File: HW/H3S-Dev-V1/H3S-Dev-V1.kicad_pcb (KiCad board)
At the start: 2 copper layers, 85 x 56 mm, 33 parts, among them J1 USB_C_Receptacle_USB2.0_16P, J2 Conn_01x02_Socket, J3 Conn_Coaxial, Q1 DMP3099L, U1 Ai-Thinker-Ra-01, U2 LTC4054ES5-4.2, U3 USBLC6-2SC6, U4 ESP32-S3-WROOM-1, U5 SY8089AAAC

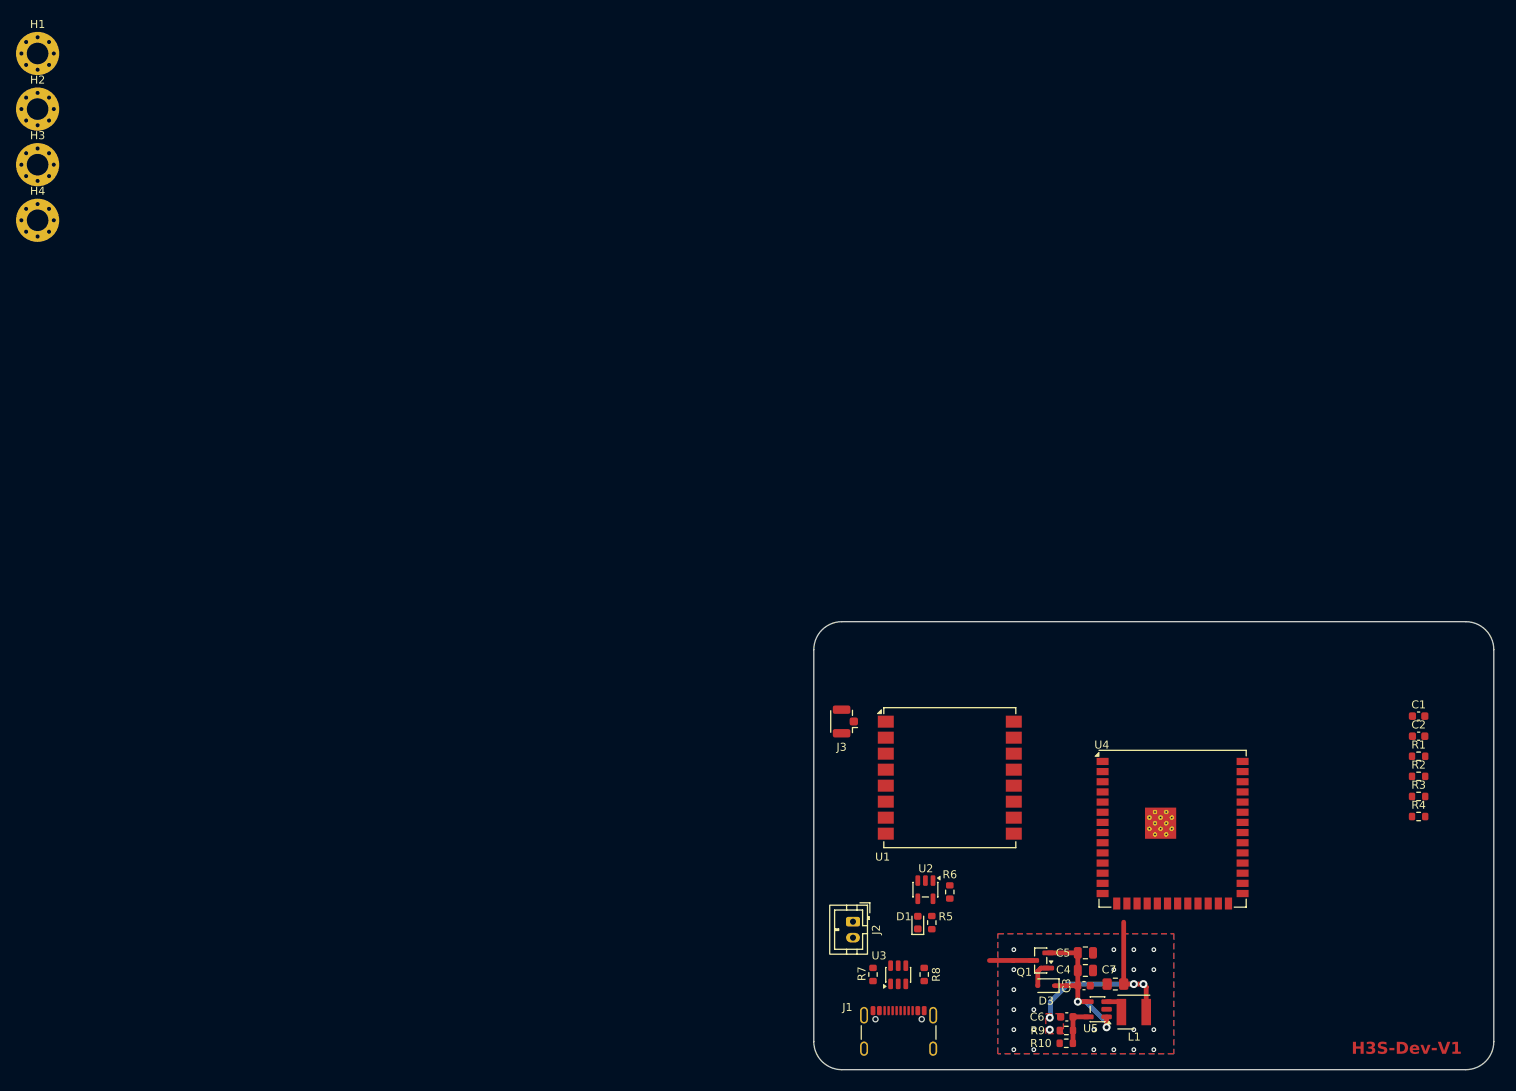
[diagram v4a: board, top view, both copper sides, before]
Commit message: LoRa, Reset and some more routing
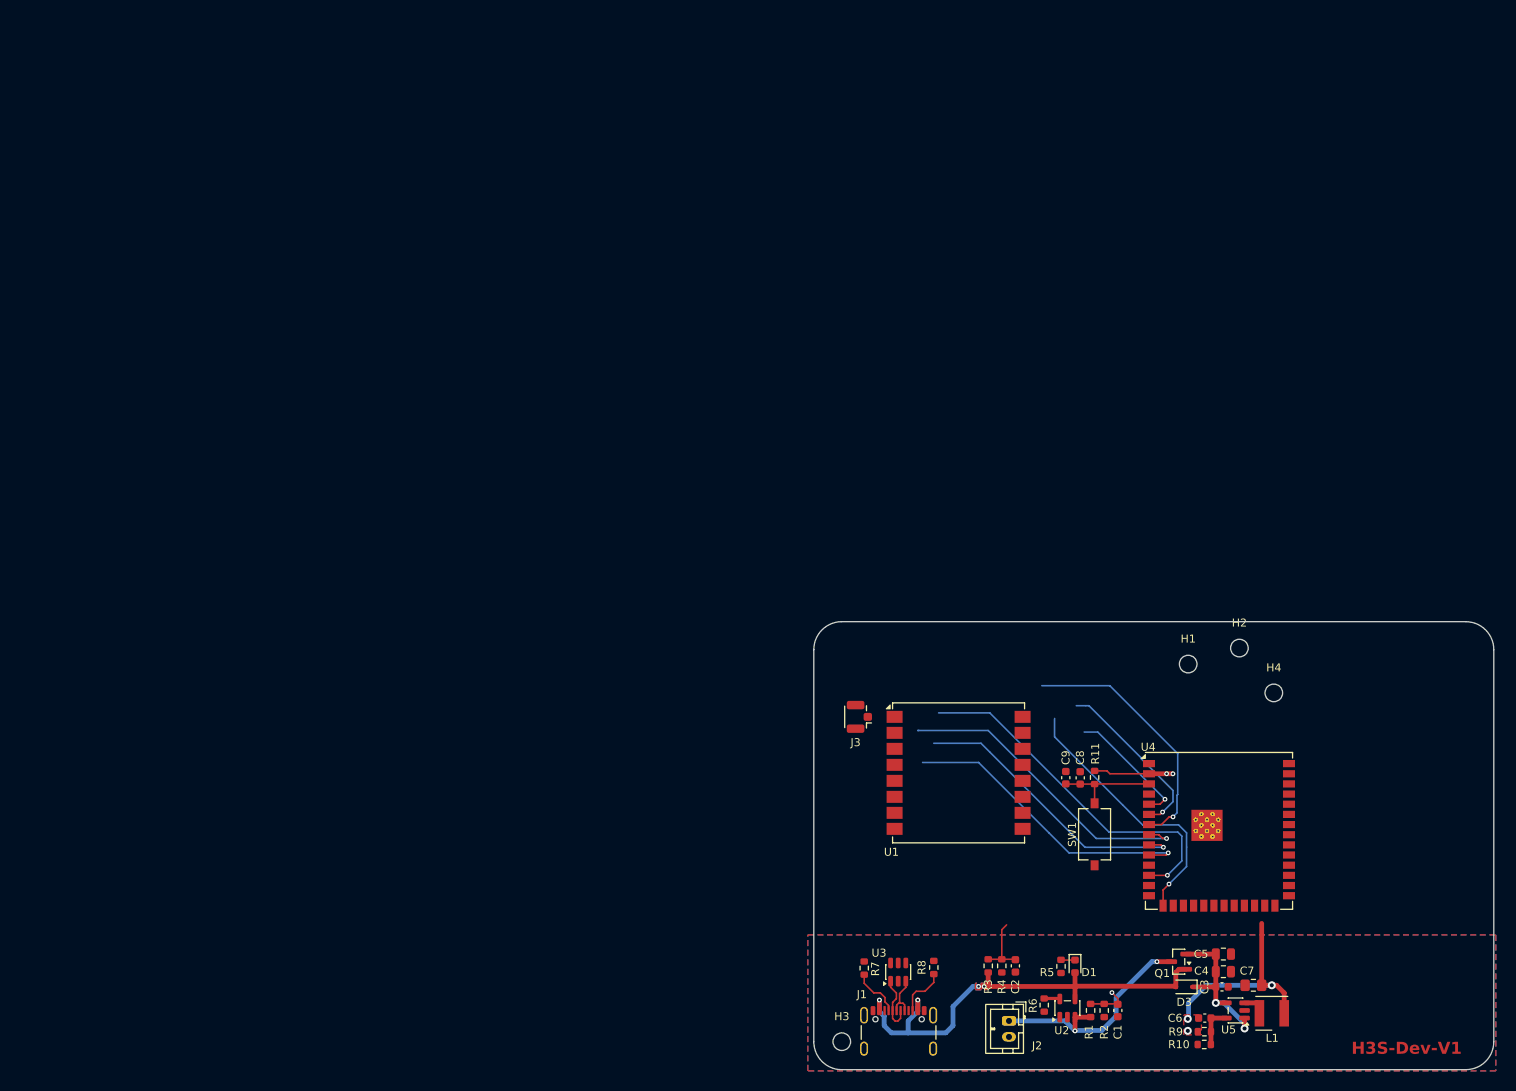
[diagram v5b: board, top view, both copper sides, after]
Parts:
- added C8: 1u, Capacitor_SMD:C_0603_1608Metric, F.Cu at (133.3, 93.5)
- added C9: 100n, Capacitor_SMD:C_0603_1608Metric, F.Cu at (131.5, 93.5)
- added R11: 10k, Resistor_SMD:R_0603_1608Metric, F.Cu at (135.1, 93.5)
- added SW1: SW_Push, Button_Switch_SMD:SW_Tactile_SPST_NO_Straight_CK_PTS636Sx25SMTRLFS, F.Cu at (135.1, 100.6)
- H1, H2, H3, H4: value MountingHole_Pad_MP -> MountingHole; footprint MountingHole:MountingHole_2.7mm_M2.5_Pad_Via -> MountingHole:MountingHole_2.2mm_M2
- moved H4 165.4 mm to (157.5, 82.9)
- moved H2 164.6 mm to (153.2, 77.3)
- moved H1 162.8 mm to (146.8, 79.3)
- moved H3 148.7 mm to (103.5, 126.5)
- moved C2 58.0 mm to (125.2, 117.0), turned to -90 degrees
- moved R3 57.8 mm to (121.8, 117.0), turned to 90 degrees
- moved R4 55.3 mm to (123.5, 117.0), turned to -90 degrees
- moved C1 52.6 mm to (138.0, 122.6), turned to -90 degrees
- moved R1 51.9 mm to (134.6, 122.6), turned to 90 degrees
- moved R2 49.0 mm to (136.3, 122.6), turned to -90 degrees
- moved U2 23.1 mm to (131.7, 122.3), turned to 90 degrees
- moved J2 23.1 mm to (124.4, 123.9)
- moved D1 20.4 mm to (132.7, 117.1), turned to -90 degrees
- moved R6 18.4 mm to (128.8, 121.9), turned to -90 degrees
- moved C3 17.3 mm to (151.0, 119.7)
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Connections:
- U1 pad 10: unconnected-(U1-DIO4-Pad10) -> /DIO4
- U1 pad 11: unconnected-(U1-DIO5-Pad11) -> /DIO5
- U1 pad 12: unconnected-(U1-SCK-Pad12) -> /SCK
- U1 pad 13: unconnected-(U1-MISO-Pad13) -> /MISO
- U1 pad 14: unconnected-(U1-MOSI-Pad14) -> /MOSI
- U1 pad 15: unconnected-(U1-~{NSS}-Pad15) -> /~{SS}
- U1 pad 4: unconnected-(U1-~{RESET}-Pad4) -> /~{LoRa_RST}
- U1 pad 5: unconnected-(U1-DIO0-Pad5) -> /DIO0
- U1 pad 6: unconnected-(U1-DIO1-Pad6) -> /DIO1
- U1 pad 7: unconnected-(U1-DIO2-Pad7) -> /DIO2
- U1 pad 8: unconnected-(U1-DIO3-Pad8) -> /DIO3
- U4 pad 10: unconnected-(U4-IO17-Pad10) -> /DIO2
- U4 pad 12: unconnected-(U4-IO8-Pad12) -> /~{LoRa_RST}
- U4 pad 15: unconnected-(U4-IO3-Pad15) -> /MISO
- U4 pad 3: unconnected-(U4-EN-Pad3) -> /~{ESP_EN}
- U4 pad 5: unconnected-(U4-IO5-Pad5) -> /SCK
- U4 pad 6: unconnected-(U4-IO6-Pad6) -> /MOSI
- U4 pad 7: unconnected-(U4-IO7-Pad7) -> /~{SS}
- U4 pad 8: unconnected-(U4-IO15-Pad8) -> /DIO0
- U4 pad 9: unconnected-(U4-IO16-Pad9) -> /DIO1
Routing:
- net /VBUS: track 3.27 -> 59.7 mm, vias 0 -> 4
- net /~{LoRa_RST}: track 0.00 -> 44.7 mm, vias 0 -> 1
- net /DIO0: track 0.00 -> 39.2 mm, vias 0 -> 1
- net /DIO2: track 0.00 -> 37.9 mm, vias 0 -> 1
- net /DIO1: track 0.00 -> 36.0 mm, vias 0 -> 1
- net /MISO: track 0.00 -> 34.1 mm, vias 0 -> 1
- net /~{SS}: track 0.00 -> 32.1 mm, vias 0 -> 1
- net /VBAT: track 5.47 -> 29.4 mm, vias 0 -> 2
- net /MOSI: track 0.00 -> 21.6 mm, vias 0 -> 1
- net /SCK: track 0.00 -> 15.8 mm, vias 0 -> 1
- net /~{ESP_EN}: track 0.00 -> 12.8 mm
- net VCC: track 27.2 -> 36.8 mm, vias 4 -> 5
- net /V5_SENSE: track 0.00 -> 7.97 mm
- net /USB_D-: track 0.00 -> 7.39 mm
- net Net-(J1-CC2): track 0.00 -> 6.31 mm
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- added copper zone on B.Cu, net /VBUS
- added copper zone on F.Cu, net /VBUS

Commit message: Some progress ...
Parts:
- moved H4 49.8 mm to (181.5, 126.5)
- moved H1 43.3 mm to (103.5, 77.5)
- moved H2 28.3 mm to (181.5, 77.5)
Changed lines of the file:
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@@
 			(at 0 -3.15 0)
 			(layer "F.SilkS")
+			(hide yes)
 			(effects
 				(font
@@
 	)
 	(footprint "MountingHole:MountingHole_2.2mm_M2"
+		(locked yes)
 		(layer "F.Cu")
-		(at 146.8 79.3)
+		(at 103.5 77.5)
 		(descr "Mounting Hole 2.2mm, M2, no annular, generated by kicad-footprint-generator mountinghole.py")
 		(tags "mountinghole M2")
@@
 			(at 0 -3.15 0)
 			(layer "F.SilkS")
+			(hide yes)
 			(effects
 				(font
@@
 		(sheetname "/")
 		(sheetfile "H3S-Dev-V1.kicad_sch")
+		(solder_mask_margin 1.1)
+		(clearance 1.1)
 		(attr exclude_from_pos_files exclude_from_bom)
 		(fp_circle
@@
 	)
 	(footprint "MountingHole:MountingHole_2.2mm_M2"
+		(locked yes)
 		(layer "F.Cu")
-		(at 157.5 82.9)
+		(at 181.5 126.5)
 		(descr "Mounting Hole 2.2mm, M2, no annular, generated by kicad-footprint-generator mountinghole.py")
 		(tags "mountinghole M2")
@@
 			(at 0 -3.15 0)
 			(layer "F.SilkS")
+			(hide yes)
 			(effects
 				(font
@@
 		(sheetname "/")
 		(sheetfile "H3S-Dev-V1.kicad_sch")
+		(solder_mask_margin 1.1)
+		(clearance 1.1)
 		(attr exclude_from_pos_files exclude_from_bom)
 		(fp_circle
@@
 	)
 	(footprint "MountingHole:MountingHole_2.2mm_M2"
+		(locked yes)
 		(layer "F.Cu")
-		(at 153.2 77.3)
+		(at 181.5 77.5)
 		(descr "Mounting Hole 2.2mm, M2, no annular, generated by kicad-footprint-generator mountinghole.py")
 		(tags "mountinghole M2")
@@
 			(at 0 -3.15 0)
 			(layer "F.SilkS")
+			(hide yes)
 			(effects
 				(font
@@
 		(sheetname "/")
 		(sheetfile "H3S-Dev-V1.kicad_sch")
+		(solder_mask_margin 1.1)
+		(clearance 1.1)
 		(attr exclude_from_pos_files exclude_from_bom)
 		(fp_circle
@@
 		)
 	)
-	(gr_rect
-		(start 167.3 126.1)
-		(end 182.1 128.4)
+	(gr_circle
+		(center 181.5 77.5)
+		(end 183.6 77.5)
 		(stroke
-			(width 0.1)
+			(width 0)
 			(type solid)
 		)
 		(fill yes)
+		(locked yes)
+		(layer "F.Mask")
+	)
+	(gr_circle
+		(center 103.5 77.5)
+		(end 105.6 77.5)
+		(stroke
+			(width 0)
+			(type solid)
+		)
+		(fill yes)
+		(locked yes)
+		(layer "F.Mask")
+	)
+	(gr_circle
+		(center 181.5 126.5)
+		(end 183.6 126.5)
+		(stroke
+			(width 0)
+			(type solid)
+		)
+		(fill yes)
+		(locked yes)
 		(layer "F.Mask")
 	)
@@
 	)
 	(gr_circle
+		(center 103.5 77.5)
+		(end 105.6 77.5)
+		(stroke
+			(width 0)
+			(type solid)
+		)
+		(fill yes)
+		(locked yes)
+		(layer "B.Mask")
+	)
+	(gr_circle
 		(center 103.5 126.5)
 		(end 105.6 126.5)
@@
 		(layer "B.Mask")
 	)
+	(gr_circle
+		(center 181.5 77.5)
+		(end 183.6 77.5)
+		(stroke
+			(width 0)
+			(type solid)
+		)
+		(fill yes)
+		(locked yes)
+		(layer "B.Mask")
+	)
+	(gr_circle
+		(center 181.5 126.5)
+		(end 183.6 126.5)
+		(stroke
+			(width 0)
+			(type solid)
+		)
+		(fill yes)
+		(locked yes)
+		(layer "B.Mask")
+	)
 	(gr_arc
 		(start 100 77.5)
@@
 	)
 	(gr_text "H3S-Dev-V1"
-		(at 167.2 128.2 0)
-		(layer "F.Cu")
+		(at 162.9 127.5 0)
+		(layer "F.Mask")
 		(effects
 			(font
@@
 		(polygon
 			(pts
-				(xy 99.25 130.15) (xy 99.25 113.15) (xy 185.25 113.15) (xy 185.25 130.15)
+				(xy 99.25 130.65) (xy 99.25 73.15) (xy 185.75 73.15) (xy 185.75 130.65)
 			)
 		)
@@
 		)
 	)
+	(group ""
+		(locked yes)
+		(members "830eea59-daa6-4248-a7af-f3a2475c1c74" "8b8aa4b0-2d80-4032-9ac5-c133dfd891e7"
+			"fb9b3bd7-be27-45a6-908c-335075aa53a4"
+		)
+	)
+	(group ""
+		(locked yes)
+		(members "06521ee4-cf1a-4ecd-af0c-9eadb0bfc367" "86974655-1a72-4c11-a6d5-d67d29e02df1"
+			"ceffec7b-a693-48fd-8e8f-6f82e61aad67"
+		)
+	)
+	(group ""
+		(locked yes)
+		(members "0bb62daa-6dae-422d-a65c-e5e318dff734" "4c95c41a-d33f-478f-86ff-c8d1a3ea1963"
+			"82eb2999-cd7f-47b5-8829-bd9fccca589c"
+		)
+	)

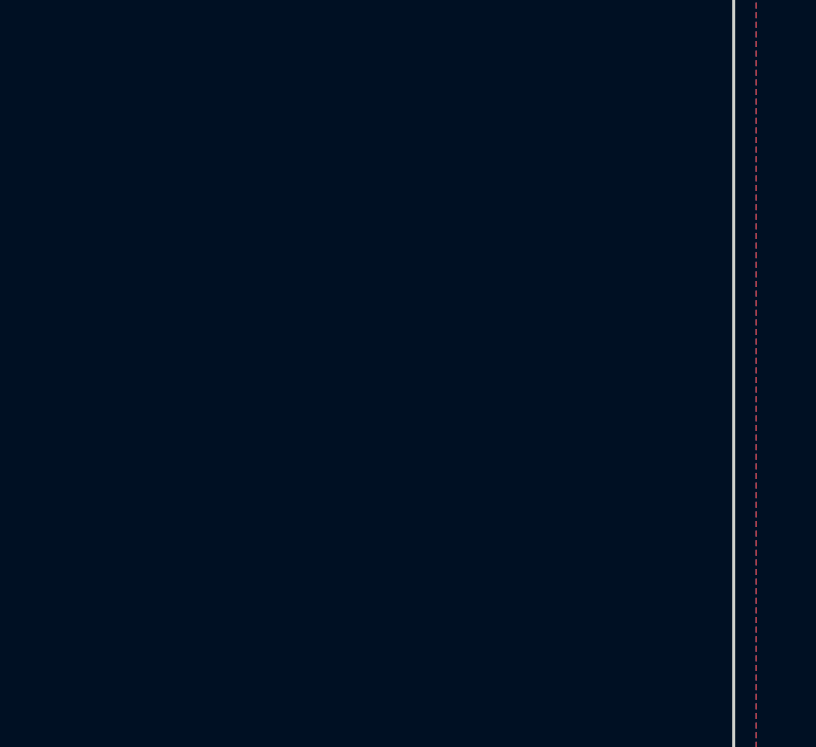
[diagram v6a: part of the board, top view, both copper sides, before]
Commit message: GNSS Module added
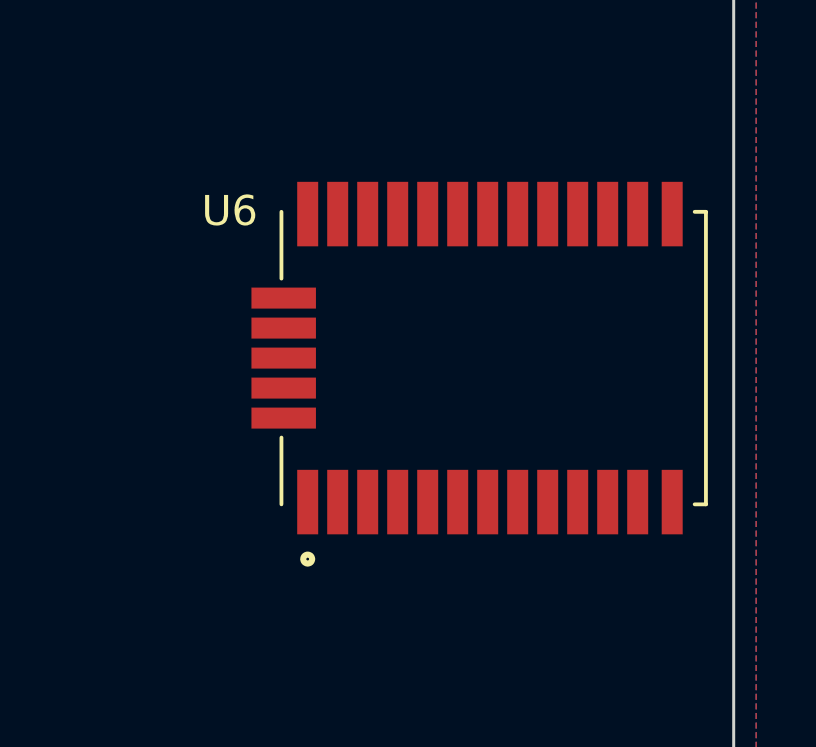
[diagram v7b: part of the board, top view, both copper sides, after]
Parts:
- added U6: L96-M33, L96_M33:XCVR_L96-M33, F.Cu at (177.0, 101.0)

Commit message: Some progress ...
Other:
- board text added: "(c) HobbyIoT H3S-Dev-V1 Helium node Meshtastic node"
- board text removed: "H3S-Dev-V1"
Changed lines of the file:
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@@
 		(layer "Margin")
 	)
-	(gr_text "H3S-Dev-V1"
-		(at 162.9 127.5 0)
+	(gr_text "(c) HobbyIoT\nH3S-Dev-V1\nHelium node\nMeshtastic node"
+		(at 183.5 118.6 0)
 		(layer "F.Mask")
 		(effects
@@
 				(bold yes)
 			)
-			(justify left bottom)
+			(justify right)
 		)
 	)
